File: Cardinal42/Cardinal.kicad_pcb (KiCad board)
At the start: 2 copper layers, 135.3 x 102.9 mm, 64 parts, among them SW1 Switch, SW10 Switch, SW11 Switch, SW12 Switch, SW13 Switch, SW14 Switch, SW15 Switch, SW16 Switch, SW17 Switch, SW18 Switch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

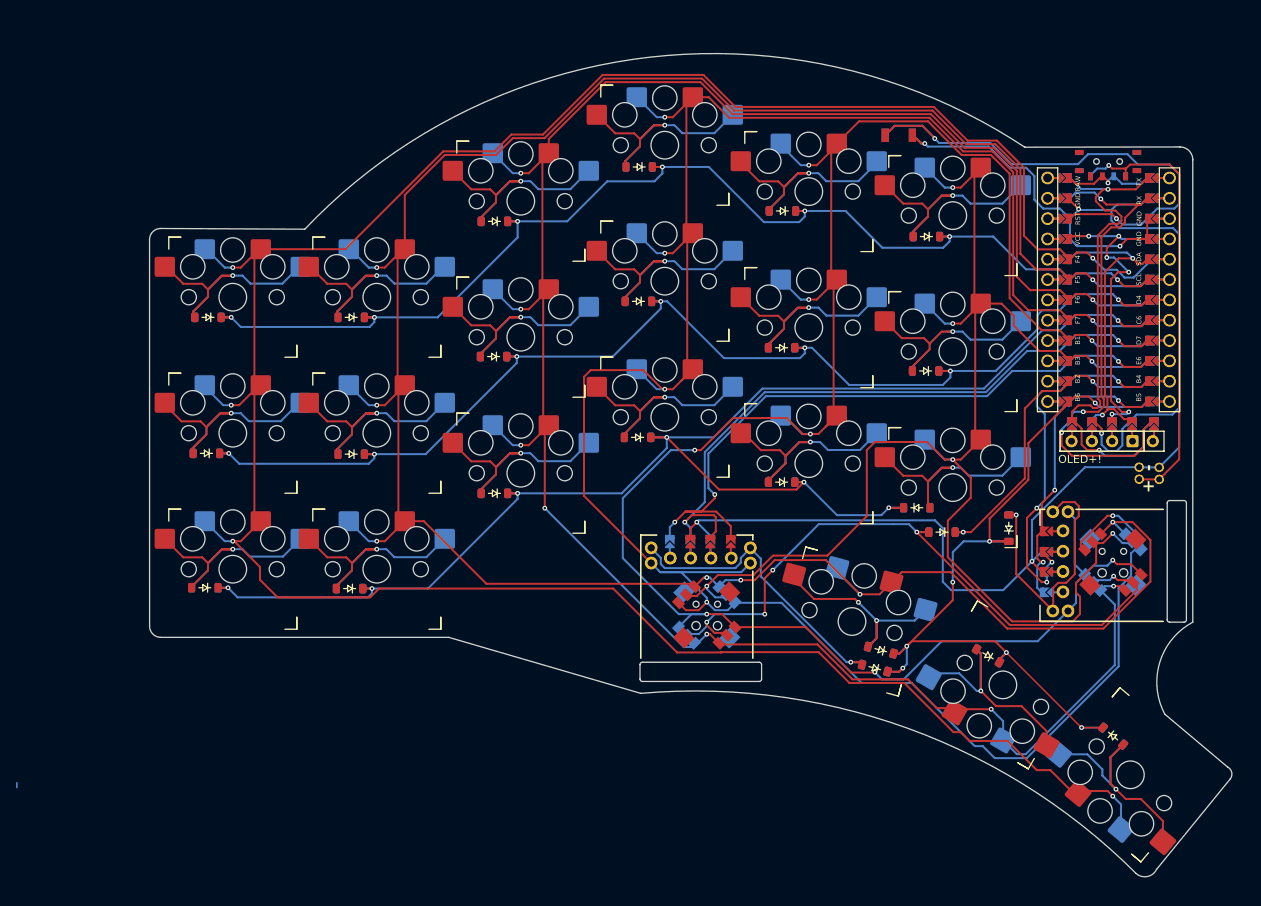
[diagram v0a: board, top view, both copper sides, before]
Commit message: Flip FIx
Fixed a lot of footprints and traces that were "upside down", my fault when i initially made the jump-pads.

Prep work done for column -1 being detachable.

Testing fill plane, no gnd/vcc for it, shouldnt be necessary.

Still planing silkscreen.
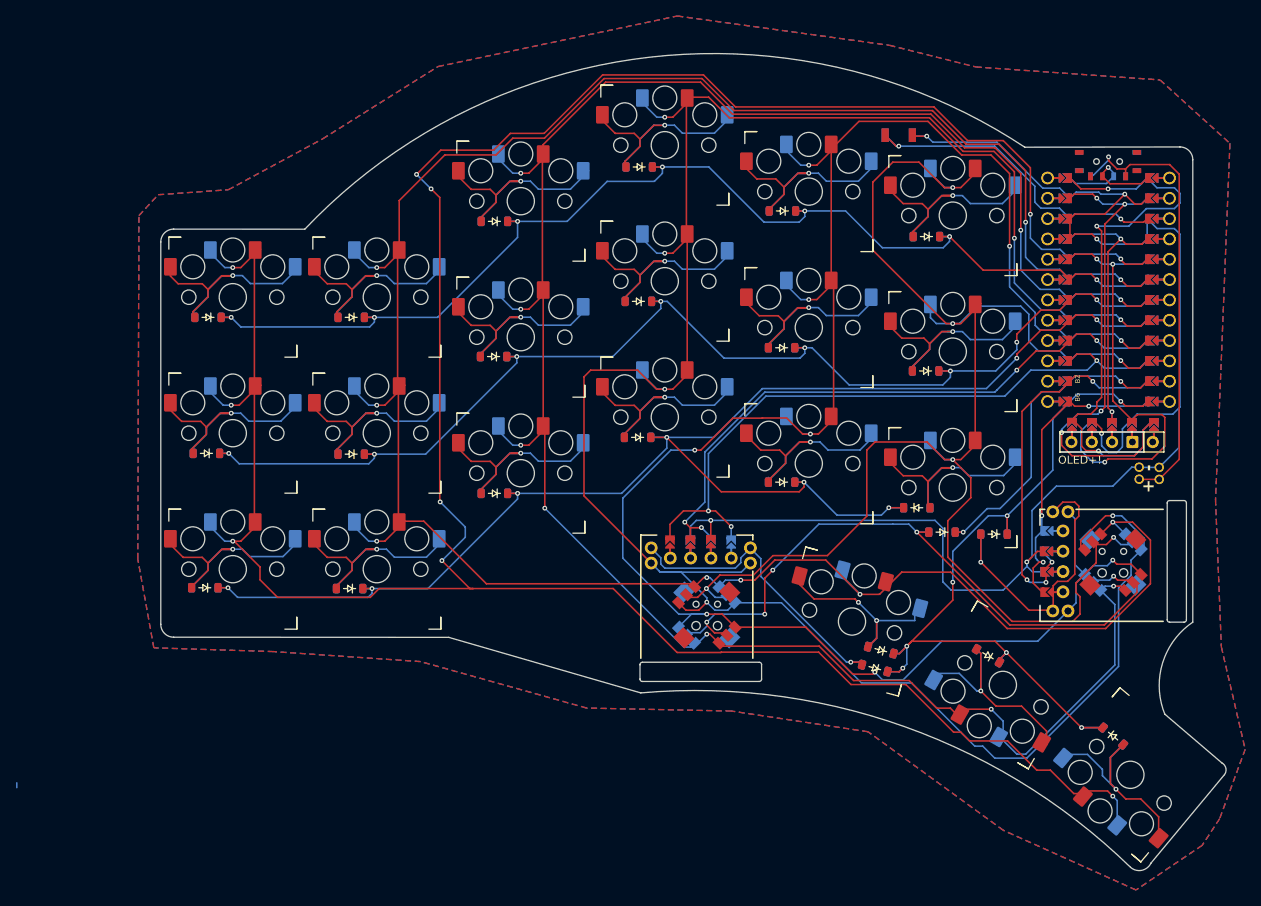
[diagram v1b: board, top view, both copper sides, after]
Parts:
- added ?: , clipboard:37a111ce-96c9-42a8-b0d1-cee97aba29f6, B.Cu at (148.4, 117.8)
- added ?: , clipboard:37a111ce-96c9-42a8-b0d1-cee97aba29f6, B.Cu at (188.1, 116.2)
- added ?: , clipboard:37a111ce-96c9-42a8-b0d1-cee97aba29f6, F.Cu at (139.7, 117.8)
- added ?: , clipboard:37a111ce-96c9-42a8-b0d1-cee97aba29f6, F.Cu at (187.1, 123.8)
- moved DT4 2.00 mm to (180.8, 116.8), turned to 180 degrees
- moved OLED+! 0.10 mm to (194.2, 105.3)
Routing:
- net Column-1: track 330.3 -> 357.6 mm, vias 5 -> 10
- net Reset: track 67.4 -> 41.3 mm
- net Column5: track 190.2 -> 210.2 mm
- net SCK/SCL: track 38.4 -> 55.6 mm, vias 2 -> 3
- net Column4: track 254.2 -> 245.2 mm, vias 8 -> 9
- net Column3: track 301.4 -> 292.6 mm, vias 6 -> 7
- net CS: track 64.3 -> 72.0 mm, vias 2 -> 3
- net Column2: track 278.0 -> 270.5 mm, vias 8 -> 9
- net VCC: track 40.8 -> 35.2 mm, vias 6 -> 2
- net EncoderB1: track 81.2 -> 77.7 mm, vias 2 -> 4
- net Column1: track 312.9 -> 309.5 mm, vias 8 -> 9
- net Net-(DT4-A): track 34.7 -> 37.5 mm
- net B+: track 12.2 -> 15.0 mm
- net MOSI/A: track 63.4 -> 61.4 mm, vias 3 -> 4
- net Net-(D14-A): track 34.9 -> 33.3 mm
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- added copper zone on B.Cu, net (none)
- added copper zone on F.Cu, net (none)
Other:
- board size 135.3 x 102.9 mm -> 133.2 x 102.1 mm

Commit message: Release: V0.9
Final desing mostly done, maybe one or two things left to refine.
Added cutouts to reduce number of keys.
Added logo.
Added support for tenting puck, only 2 screws and maybe removed latter.
Tweaked traces.
Tested for plated holes, not convinced enough, changing in future version should be easy, but could make manufacturing problems due to the spacing from holes to pads.

Added gerber files autogenerated with kicad, a board should be in the making.
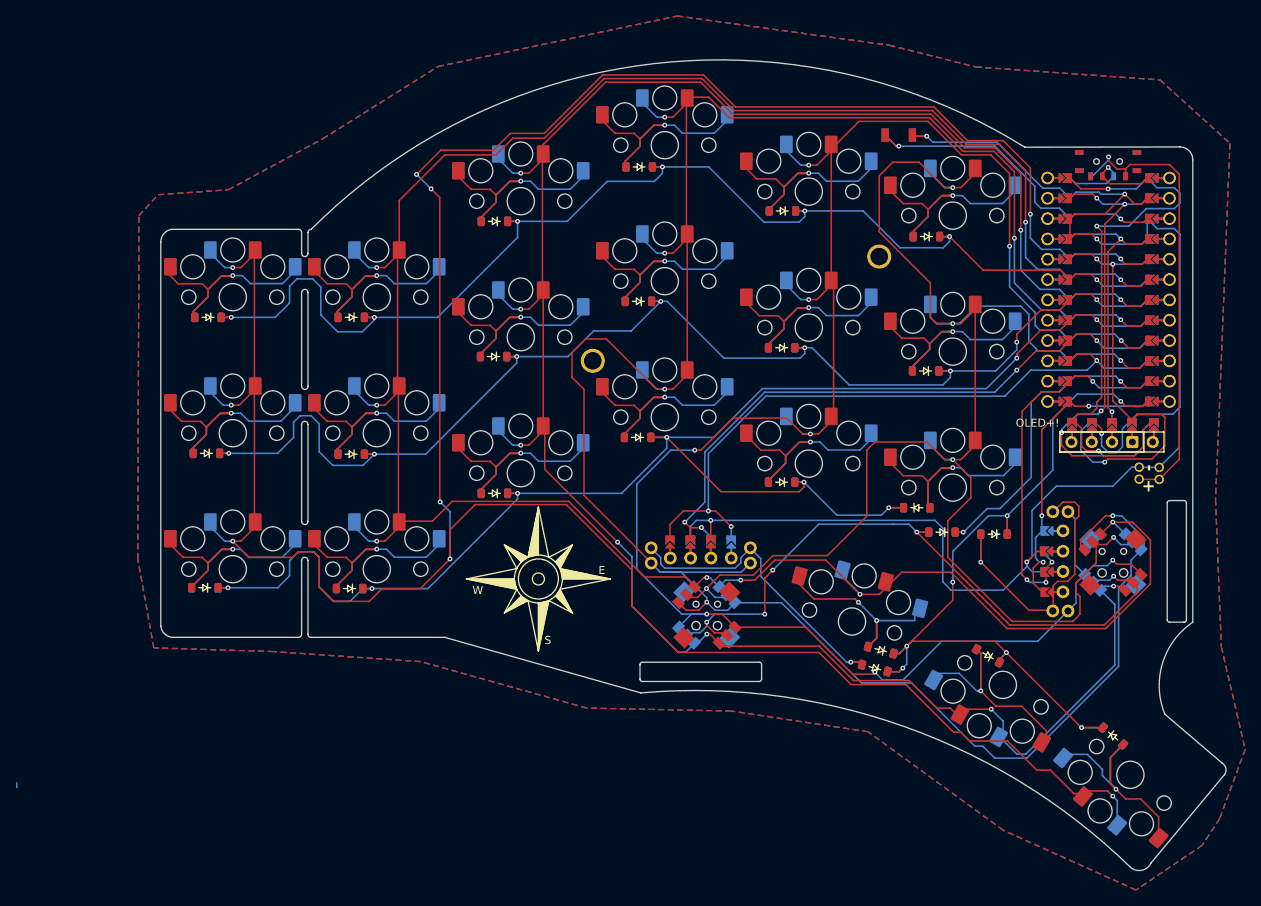
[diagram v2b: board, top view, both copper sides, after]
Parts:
- added REF**: Tenting Puck, PCM_marbastlib-various:SplitkbTentingPuck, F.Cu at (148.5, 88.6)
- added REF**: Cardinal, mine:Cardinal, F.Cu at (123.8, 122.4)
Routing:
- net Column-1: track 357.6 -> 365.7 mm
- net row1: track 150.2 -> 157.8 mm
- net Column3: track 292.6 -> 299.7 mm
- net row2: track 153.1 -> 159.5 mm
- net row3: track 183.6 -> 189.5 mm
- net Column1: track 309.5 -> 311.6 mm
- net Column4: track 245.2 -> 243.5 mm
- net Column2: track 270.5 -> 271.8 mm
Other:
- board size 133.2 x 102.1 mm -> 133.2 x 101.3 mm
- board text added: "OLED+!"

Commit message: Minor update
Minor update to footprints/size
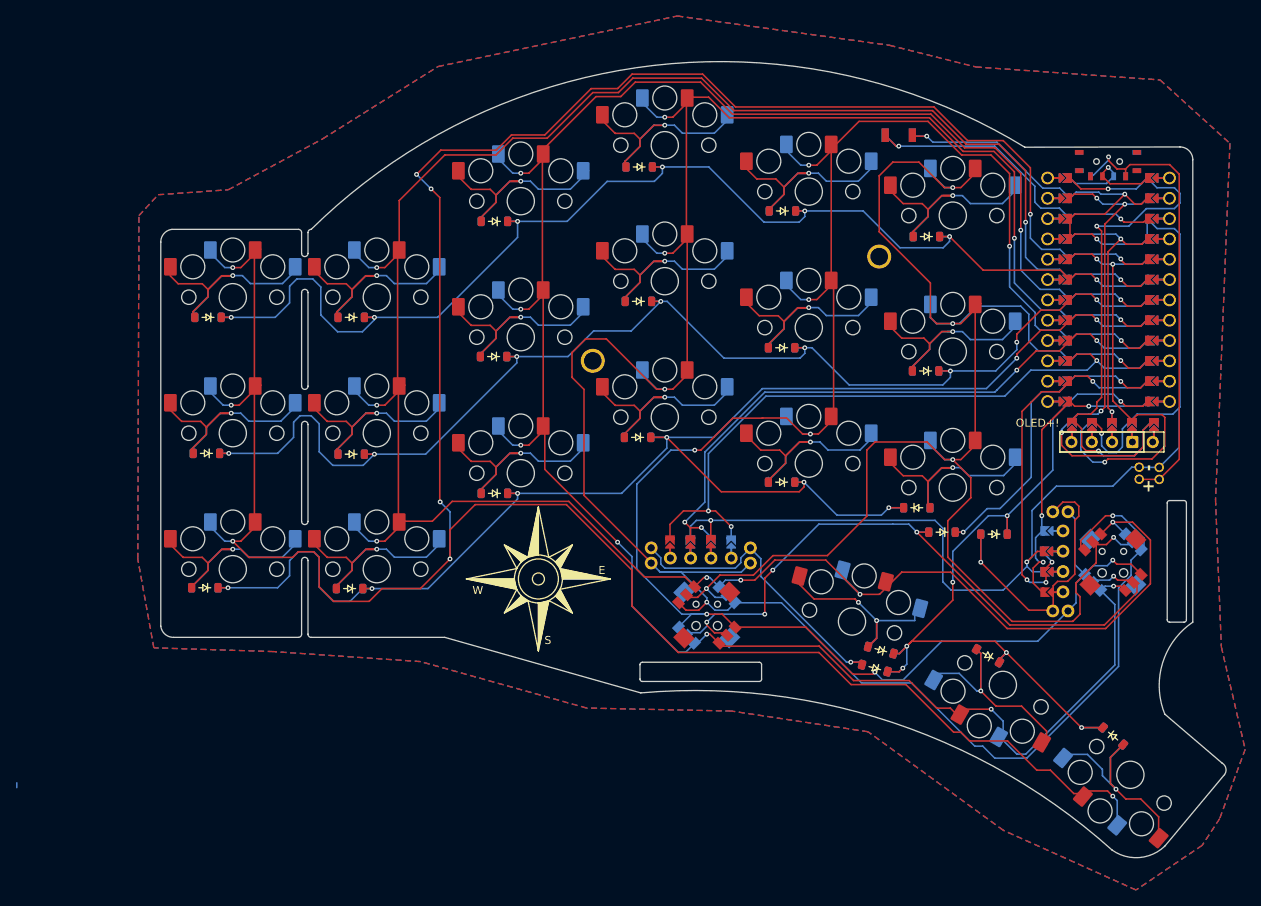
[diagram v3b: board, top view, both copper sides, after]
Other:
- board size 133.2 x 101.3 mm -> 133.2 x 99.5 mm

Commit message: Update PCB V0.99
After ordering pcbs and while testing then i noticed one of the pads its not conected, fixed now, at least its from one of the switches and i can add a jumper to it
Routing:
- net Column4: track 243.5 -> 246.6 mm
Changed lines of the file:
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@@
   (segment (start 195.6 120.05) (end 194.906497 120.743503) (width 0.2) (layer "B.Cu") (net 25))
   (segment (start 144.85 126.8) (end 141.725 126.8) (width 0.2) (layer "B.Cu") (net 25))
-  (segment (start 156.8 104.28) (end 157.8 104.28) (width 0.2) (layer "B.Cu") (net 25))
   (segment (start 190.85 120.593314) (end 190.85 114.85) (width 0.2) (layer "B.Cu") (net 25))
+  (segment (start 156.78 104.28) (end 154.8 102.3) (width 0.2) (layer "B.Cu") (net 25))
   (segment (start 136.1 110.55) (end 140.35 106.3) (width 0.2) (layer "B.Cu") (net 25))
   (segment (start 182.7 80.8) (end 182.7 85.9) (width 0.2) (layer "B.Cu") (net 25))
@@
   (segment (start 192.076966 121.82028) (end 190.85 120.593314) (width 0.2) (layer "B.Cu") (net 25))
   (segment (start 185.9 90.7) (end 186.5 91.3) (width 0.2) (layer "B.Cu") (net 25))
+  (segment (start 157.8 104.28) (end 156.78 104.28) (width 0.2) (layer "B.Cu") (net 25))
   (segment (start 196.65 92.6) (end 195.85 91.8) (width 0.2) (layer "B.Cu") (net 25))
   (segment (start 156.6 70.68) (end 154.8 68.88) (width 0.2) (layer "B.Cu") (net 25))
+  (segment (start 154.8 102.3) (end 154.8 102.08) (width 0.2) (layer "B.Cu") (net 25))
   (segment (start 193.153743 120.743503) (end 192.076966 121.82028) (width 0.2) (layer "B.Cu") (net 25))
   (segment (start 194.906497 120.743503) (end 193.153743 120.743503) (width 0.2) (layer "B.Cu") (net 25))

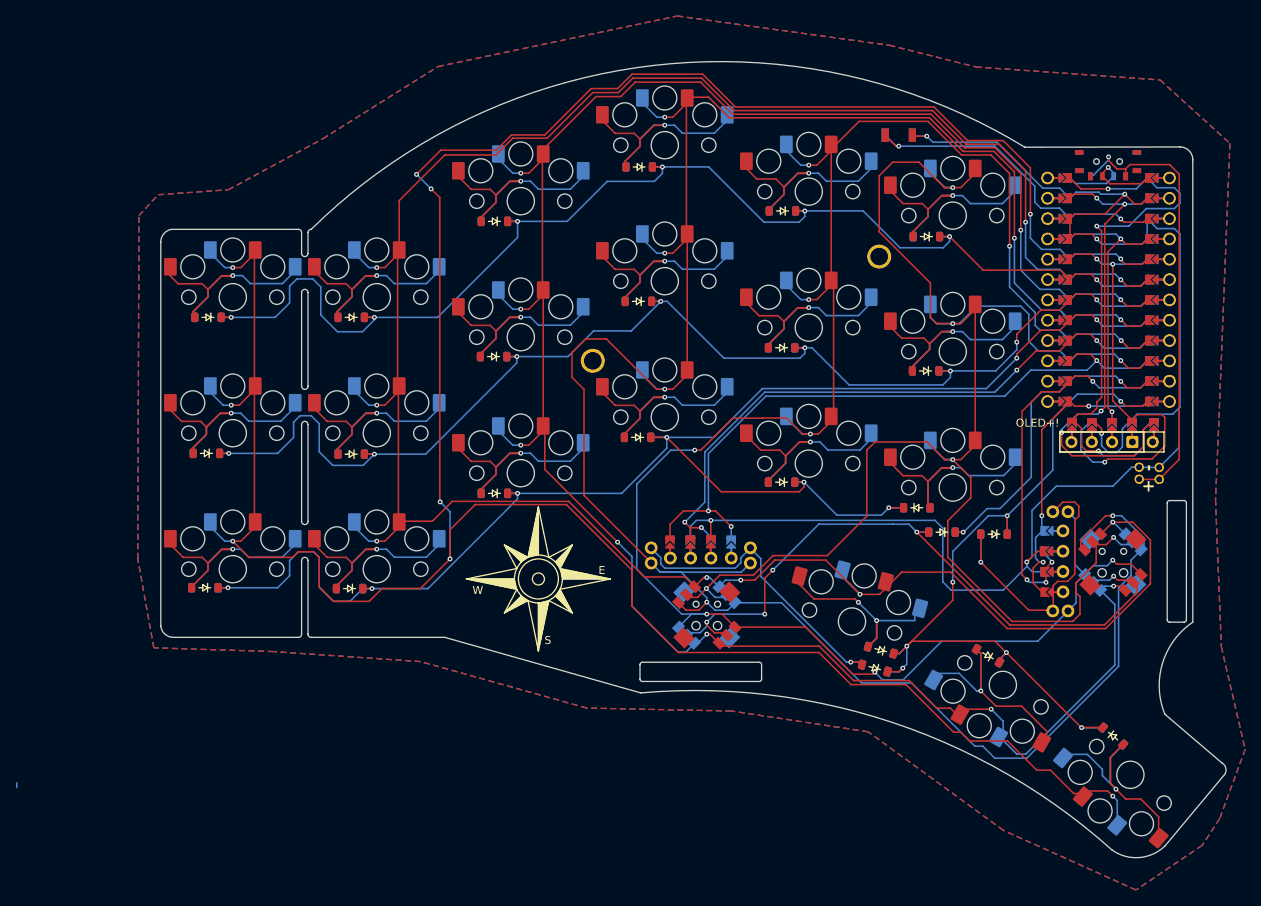
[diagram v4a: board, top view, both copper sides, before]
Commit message: Probably V1
Most likely this will be the release 1.0 for now on, after fixing 2 wrong traces in the desing, luckily things were an easy fix cutting a trace and adding a wire
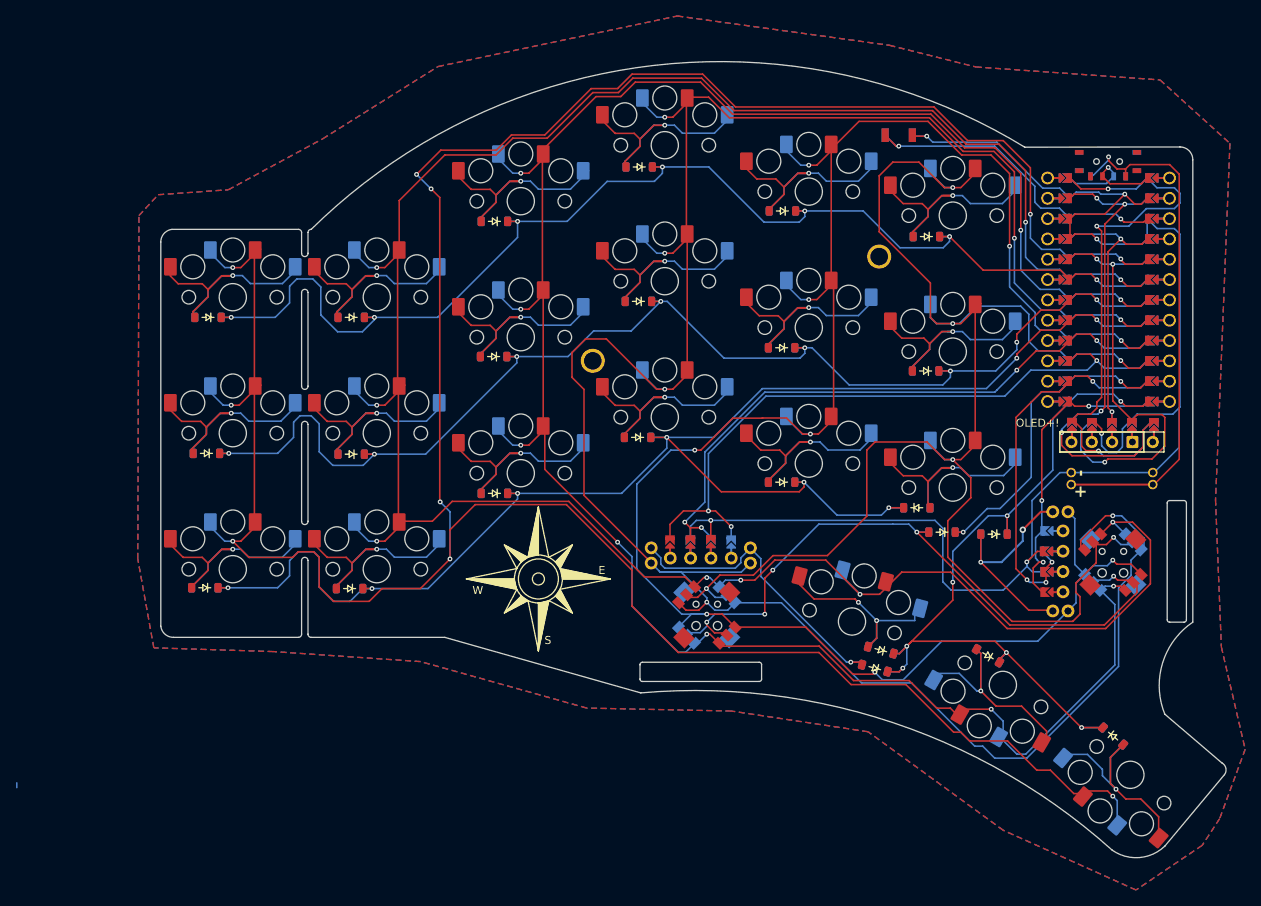
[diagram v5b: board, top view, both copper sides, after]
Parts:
- moved BT1 8.53 mm to (192.4, 109.8)
- moved BT1 1.03 mm to (198.6, 109.8)
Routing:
- net Net-(BT1-+): track 56.4 -> 65.1 mm
- net Net-(DT4-A): track 37.5 -> 31.0 mm, vias 1 -> 2
- net gnd: track 197.4 -> 198.2 mm
- net EncoderB2: track 47.4 -> 48.1 mm
- net Net-(D14-A): track 33.3 -> 32.7 mm
